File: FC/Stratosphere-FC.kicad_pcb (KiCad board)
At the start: 2 copper layers, 52.2 x 84.1 mm, 95 parts, among them J1 Conn_01x04, J1 Connector, J2 Conn_01x04, J2 SPI3, J3 Conn_01x04, J4 Conn_01x04, J5 Conn_01x04, J6 Conn_01x05, J7 Conn_01x04, P2 USB_C_Plug_USB2.0, U1 ICM-42605, U2 W25Q16JVSS, U3 BMP388, U4 XC6206P332MR, U5 AMS1117, U8 STM32F405RGTx, X2 Shenzhen SCTF Elec SX2B12.000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

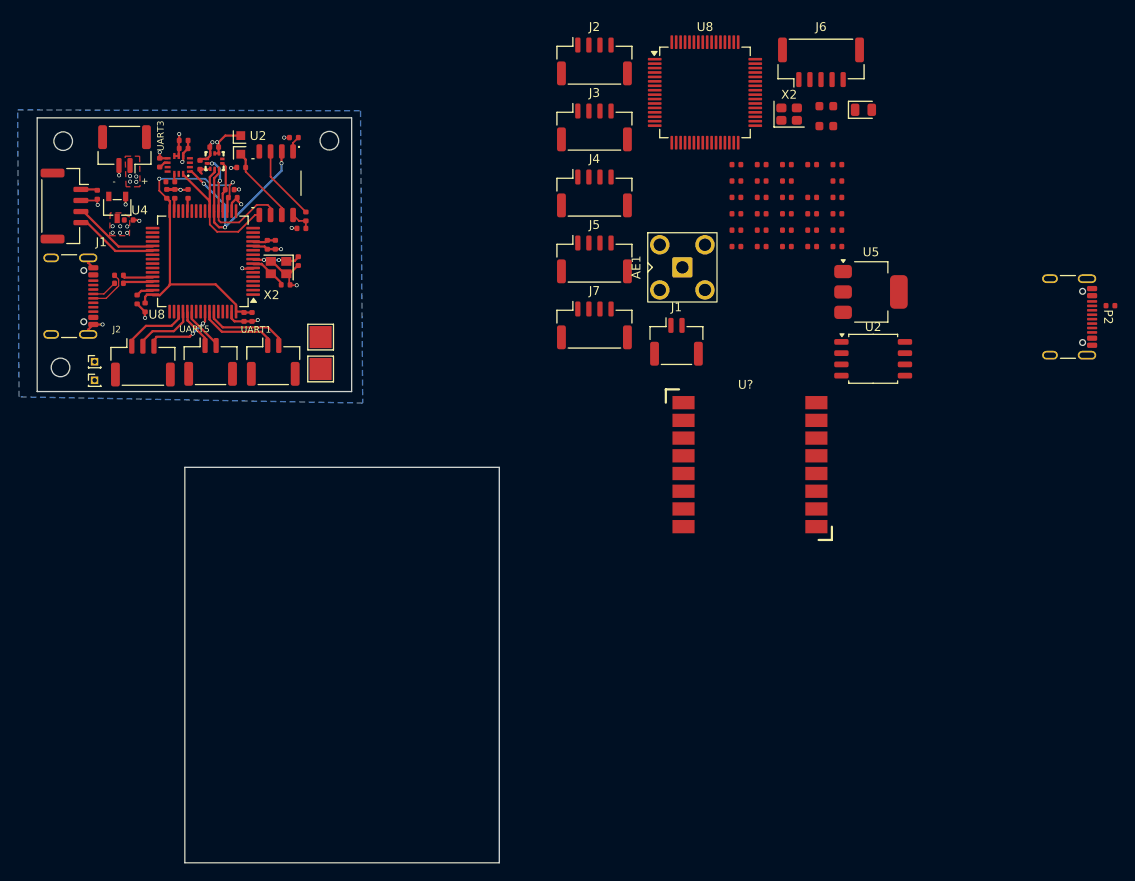
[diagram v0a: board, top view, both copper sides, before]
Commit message: fix: updated connector, horzontal to vertical
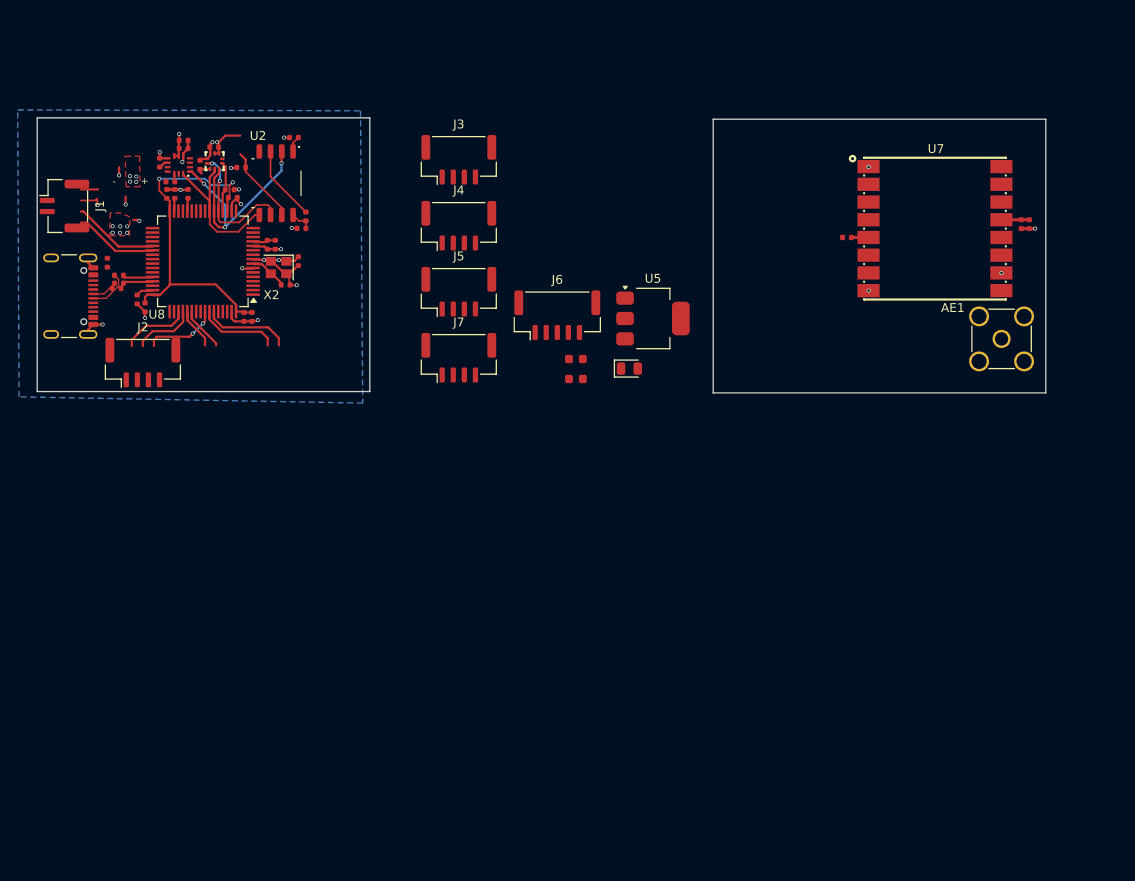
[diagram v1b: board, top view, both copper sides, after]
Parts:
- removed the C1 at (191.5, 63.1)
- removed the C12 at (194.4, 63.1)
- removed the C13 at (194.4, 64.9)
- removed the C14 at (194.4, 66.8)
- removed the C16 at (194.4, 68.6)
- removed the C17 at (194.4, 70.5)
- removed the C19 at (194.4, 72.3)
- removed the C2 at (191.5, 64.9)
- removed the C22 at (197.2, 63.1)
- removed the C23 at (197.2, 64.9)
- removed the C24 at (197.2, 66.8)
- removed the C30 at (197.2, 70.5)
- removed the C32 at (197.2, 72.3)
- removed the C33 at (200.1, 63.1)
- removed C34, C35: 1uF, PCM_JLCPCB:C_0402
- removed the C6 at (191.5, 68.6)
- removed the C7 at (191.5, 70.5)
- removed the C8 at (191.5, 72.3)
- removed the J1 at (184.8, 83.1)
- removed the J2 at (175.5, 51.4)
- removed the P2 at (228.0, 80.3)
- removed the R12 at (202.9, 66.8)
- removed the R15 at (202.9, 68.6)
- removed the R16 at (202.9, 70.5)
- removed the R17 at (202.9, 72.3)
- removed the R3 at (200.1, 66.8)
- removed the R4 at (200.1, 68.6)
- removed the R7 at (200.1, 70.5)
- removed the R9 at (200.1, 72.3)
- removed REF** (x2): TestPoint_Pad_1.0x1.0mm, TestPoint:TestPoint_Pad_1.0x1.0mm
- removed REF** (x2): PinHeader_1x01_P1.00mm_Vertical, Connector_PinHeader_1.00mm:PinHeader_1x01_P1.00mm_Vertical
- removed REF** (x2): TestPoint_Pad_2.5x2.5mm, TestPoint:TestPoint_Pad_2.5x2.5mm
- removed REF** (x3): MountingHole_2.1mm, MountingHole:MountingHole_2.1mm
- removed the U2 at (207.0, 85.0)
- removed U4: XC6206P332MR, easyeda2kicad:SOT-23-3_L2.9-W1.6-P1.90-LS2.8-BR
- removed the U8 at (188.0, 54.9)
- removed U?: COMM-SMD_LORA1276-C1-915MHZ, lib:COMM-SMD_LORA1276-C1-915MHZ
- removed UART1, UART3, UART5: Connector, Connector_JST:JST_GH_SM02B-GHS-TB_1x02-1MP_P1.25mm_Horizontal
- removed the X2 at (197.5, 57.4)
- added U7: 915MHz, lib:COMM-SMD_LORA1276-C1-915MHZ, F.Cu at (213.9, 70.3)
- AE1: footprint Connector_Coaxial:SMA_BAT_Wireless_BWSMA-KWE-Z001 -> Connector_Coaxial:SMA_Amphenol_901-144_Vertical
- J1: value Conn_01x04 -> Connector; footprint Connector_JST:JST_GH_SM04B-GHS-TB_1x04-1MP_P1.25mm_Horizontal -> Connector_JST:JST_GH_BM02B-GHS-TBT_1x02-1MP_P1.25mm_Vertical
- J2: value SPI3 -> Conn_01x04; footprint Connector_JST:JST_GH_SM03B-GHS-TB_1x03-1MP_P1.25mm_Horizontal -> Connector_JST:JST_GH_BM04B-GHS-TBT_1x04-1MP_P1.25mm_Vertical
- J3, J4, J5, J7: footprint Connector_JST:JST_GH_SM04B-GHS-TB_1x04-1MP_P1.25mm_Horizontal -> Connector_JST:JST_GH_BM04B-GHS-TBT_1x04-1MP_P1.25mm_Vertical
- moved R1 113.4 mm to (120.5, 74.2), turned to -90 degrees
- moved R11 82.3 mm to (121.5, 77.0), turned to 180 degrees
- moved J6 41.2 mm to (171.3, 80.1)
- moved C4 40.2 mm to (173.4, 85.0)
- moved C5 40.2 mm to (173.4, 87.3)
- moved D3 39.4 mm to (179.4, 86.1)
- moved AE1 36.9 mm to (221.5, 82.8)
- moved C3 33.2 mm to (224.6, 69.8), turned to -90 degrees
- moved C28 26.5 mm to (223.7, 69.8), turned to -90 degrees
- moved U5 24.8 mm to (182.1, 80.5)
- moved J3 15.7 mm to (160.2, 62.5)
- moved J7 15.7 mm to (160.2, 84.9)
- moved J4 15.7 mm to (160.2, 70.0)
- moved J5 15.7 mm to (160.2, 77.4)
- moved R10 8.30 mm to (204.0, 71.3)
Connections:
- J1 pad 1: +5V -> +3.3V
- J2 pad 1: /SPI3_SCK -> /PWM_1
- J2 pad 2: /SPI3_MISO -> /PWM_2
- J2 pad 3: /SPI3_MOSI -> /PWM_3
- R10 pad 2: /SPI1_NSS -> /SPI3_NSS
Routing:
- net +3.3V: track 11.6 -> 19.5 mm, vias 16 -> 17
- net +5V: track 1.94 -> 0.00 mm
- net /SPI3_NSS: track 0.00 -> 1.94 mm
- net GND: track 41.2 -> 40.0 mm, vias 14 -> 17
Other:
- board size 52.2 x 84.1 mm -> 113.9 x 31.1 mm
